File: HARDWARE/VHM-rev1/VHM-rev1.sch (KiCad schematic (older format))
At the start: 10 parts, among them J1 RJ45, J2 USB_C_Receptacle, Q1 DMG2301L, U1 TLP127, U2 CH340G, U3 ESP32-WROOM-32

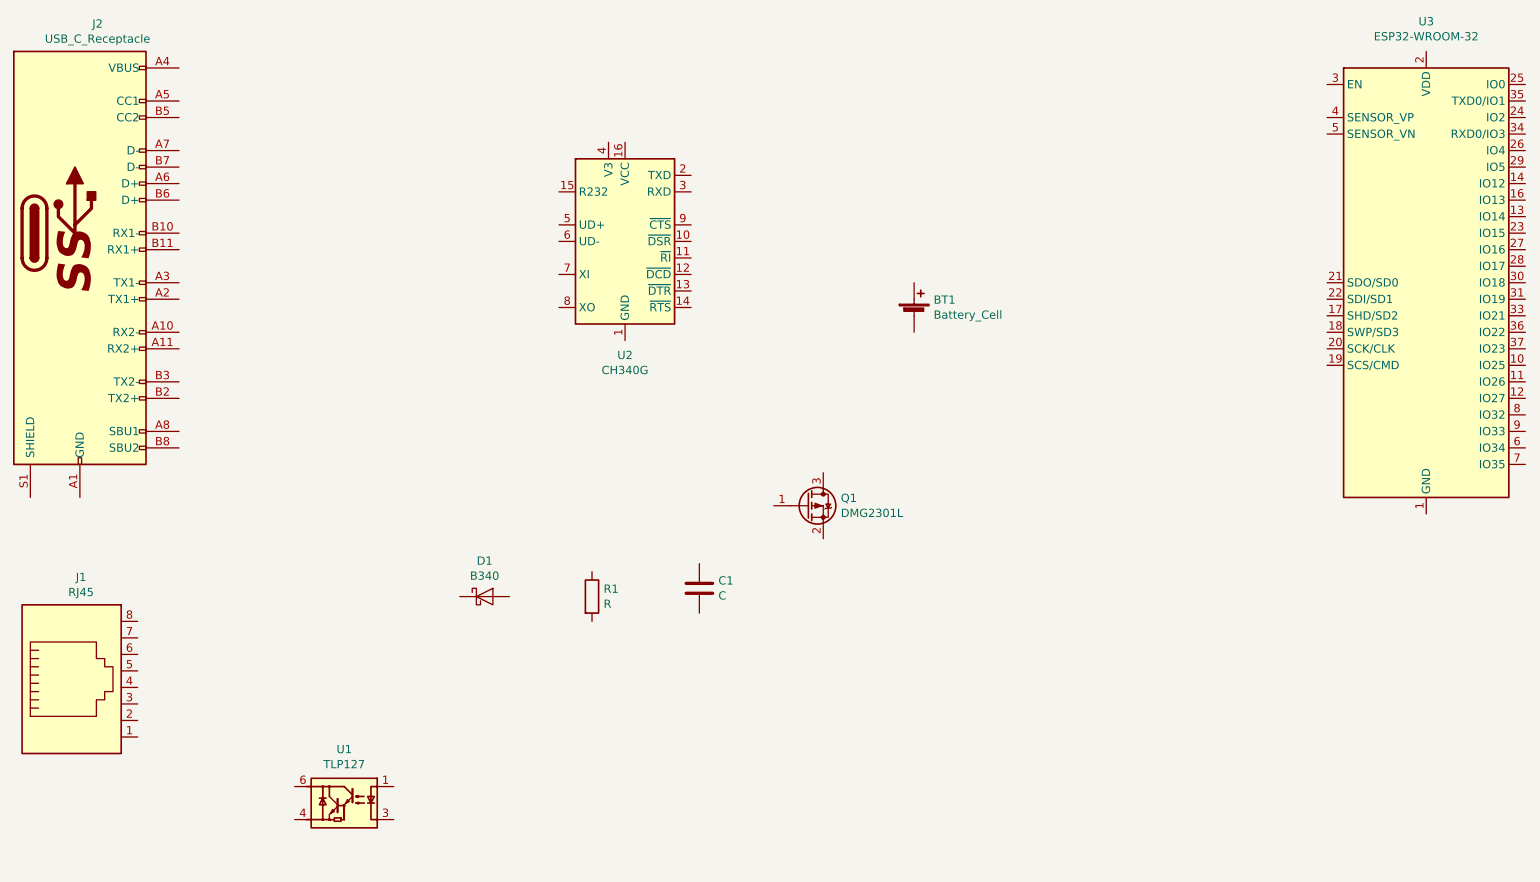
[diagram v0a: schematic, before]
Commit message: Added 3d objects and libraries
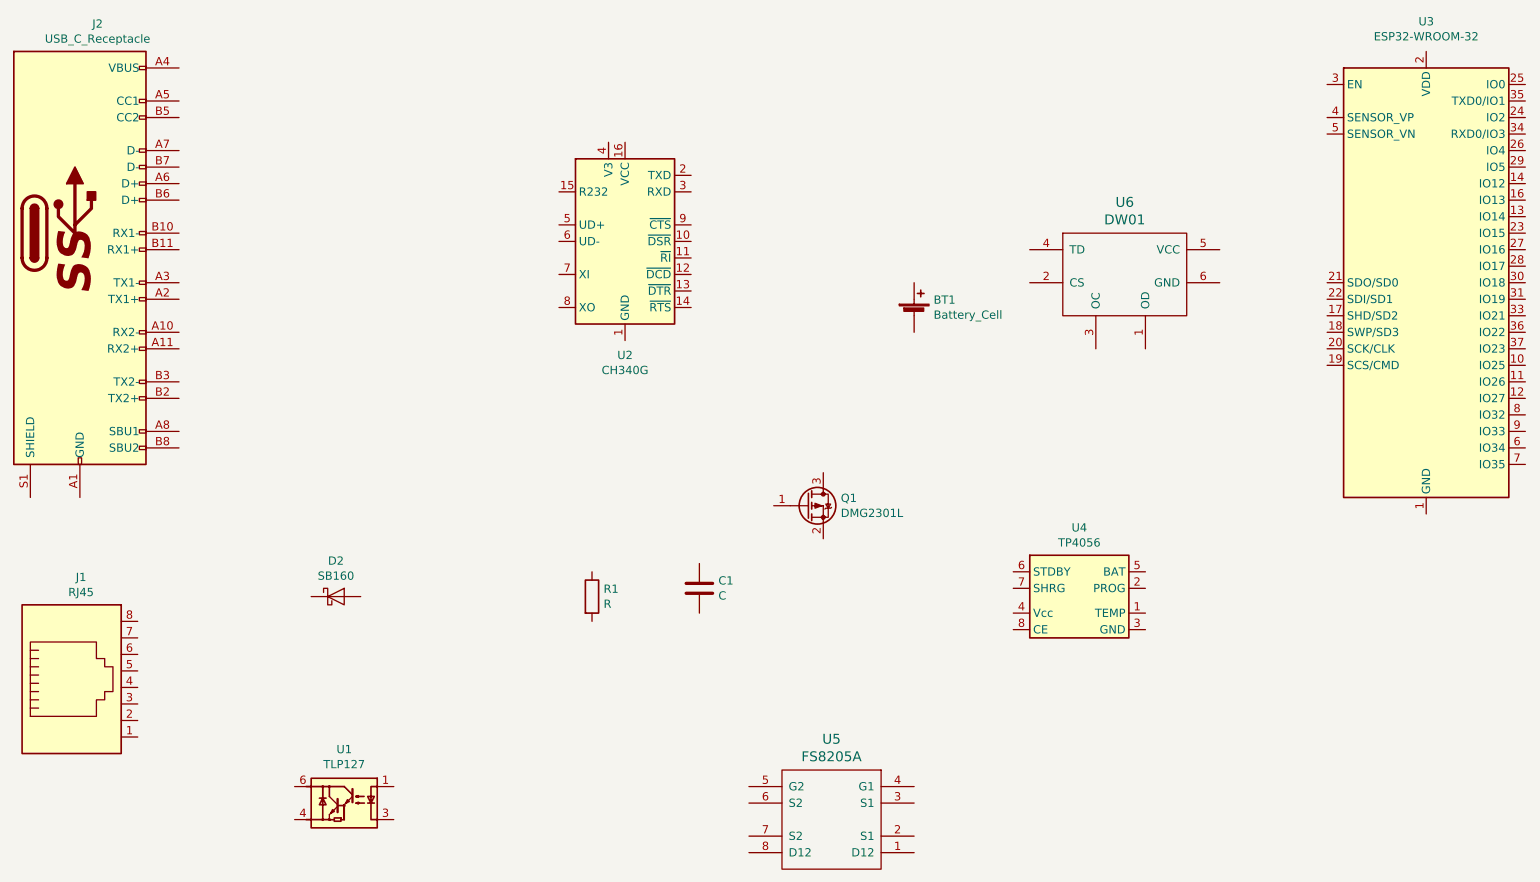
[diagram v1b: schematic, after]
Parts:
- removed D1: B340, Diodes_SMD:D_SMC, symbol Diode:B340
- added D2: SB160, Diodes_SMD:D_SMA, symbol Diode:SB160
- added U4: TP4056, lib:TP4056_SOP-8-PP, symbol Battery_Management:TP4056
- added U5: FS8205A, Housings_SSOP:TSSOP-8_4.4x3mm_Pitch0.65mm, symbol fs8205a:FS8205A
- added U6: DW01, TO_SOT_Packages_SMD:SOT-23-6_Handsoldering, symbol dw01:DW01
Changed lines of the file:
@@
-$EndComp
-$Comp
-L Diode:B340 D1
-U 1 1 5DE056AB
-P 3650 4100
-F 0 "D1" H 3650 4316 50  0000 C CNN
-F 1 "B340" H 3650 4225 50  0000 C CNN
-F 2 "Diodes_SMD:D_SMC" H 3650 3925 50  0001 C CNN
-F 3 "http://www.jameco.com/Jameco/Products/ProdDS/1538777.pdf" H 3650 4100 50  0001 C CNN
-	1    3650 4100
-	1    0    0    -1
 $EndComp
 $Comp
@@
 	1    0    0    -1
 $EndComp
+$Comp
+L Battery_Management:TP4056 U4
+U 1 1 5DE1EF07
+P 7250 4150
+F 0 "U4" H 7250 4617 50  0000 C CNN
+F 1 "TP4056" H 7250 4526 50  0000 C CNN
+F 2 "lib:TP4056_SOP-8-PP" H 7250 3800 50  0001 C CNN
+F 3 "http://beriled.biz/data/files/tp4056new.pdf" H 7250 3600 50  0001 C CNN
+	1    7250 4150
+	1    0    0    -1
+$EndComp
+$Comp
+L fs8205a:FS8205A U5
+U 1 1 5DE1A501
+P 5850 5450
+F 0 "U5" V 5363 5350 60  0000 C CNN
+F 1 "FS8205A" V 5469 5350 60  0000 C CNN
+F 2 "Housings_SSOP:TSSOP-8_4.4x3mm_Pitch0.65mm" H 6800 5700 60  0001 C CNN
+F 3 "" H 6800 5700 60  0001 C CNN
+	1    5850 5450
+	0    1    1    0
+$EndComp
+$Comp
+L dw01:DW01 U6
+U 1 1 5DE19887
+P 7500 2150
+F 0 "U6" H 7525 2587 60  0000 C CNN
+F 1 "DW01" H 7525 2481 60  0000 C CNN
+F 2 "TO_SOT_Packages_SMD:SOT-23-6_Handsoldering" H 7450 1850 60  0001 C CNN
+F 3 "" H 7450 1850 60  0001 C CNN
+	1    7500 2150
+	1    0    0    -1
+$EndComp
+$Comp
+L Diode:SB160 D2
+U 1 1 5DE1AC25
+P 2750 4100
+F 0 "D2" H 2750 4316 50  0000 C CNN
+F 1 "SB160" H 2750 4225 50  0000 C CNN
+F 2 "Diodes_SMD:D_SMA" H 2750 3925 50  0001 C CNN
+F 3 "http://www.diodes.com/_files/datasheets/ds23022.pdf" H 2750 4100 50  0001 C CNN
+	1    2750 4100
+	1    0    0    -1
+$EndComp
